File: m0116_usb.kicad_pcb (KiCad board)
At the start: 2 copper layers, 372.1 x 113.8 mm, 184 parts, among them J1 AVR-ISP-6, J2 Conn_01x04, J3 Conn_01x04, U1 ATmega32A-PU

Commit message: change ucontroller to ATmega32u4
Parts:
- D10, D11, D12, D13, D14, D15, D16, D17, D18, D19, D20, D21, D22, D23, D24, D25, D26, D27, D28, D29, D3, D30, D31, D32, D33, D34, D35, D36, D37, D38, D39, D4, D40, D41, D42, D43, D44, D45, D46, D47, D48, D49, D5, D50, D51, D52, D53, D54, D55, D56, D57, D58, D59, D6, D60, D61, D62, D63, D64, D65, D66, D67, D68, D69, D7, D70, D71, D72, D73, D74, D75, D76, D77, D78, D79, D8, D80, D81, D82, D83, D9: footprint Diode_THT:D_DO-35_SOD27_P7.62mm_Horizontal -> Diode_SMD:D_SOD-123
- MX1, MX10, MX11, MX12, MX13, MX14, MX15, MX16, MX17, MX18, MX19, MX2, MX20, MX21, MX22, MX23, MX24, MX25, MX26, MX27, MX28, MX29, MX3, MX30, MX31, MX32, MX33, MX34, MX35, MX36, MX37, MX38, MX39, MX4, MX40, MX41, MX42, MX43, MX44, MX45, MX46, MX47, MX48, MX49, MX5, MX50, MX51, MX52, MX53, MX54, MX55, MX56, MX57, MX58, MX59, MX6, MX60, MX61, MX62, MX63, MX64, MX65, MX66, MX67, MX68, MX69, MX7, MX70, MX71, MX72, MX73, MX74, MX75, MX76, MX77, MX78, MX79, MX8, MX80, MX81, MX9: footprint Alps_Only:ALPS-1U -> project_custom_parts:ALPS-1U
- USB1: footprint random-keyboard-parts:Molex-0548190519 -> project_custom_parts:Molex-0548190519
- renumbered Boot to Boot1, Reset to Reset1
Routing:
- net row4: track 532.5 -> 502.9 mm
- net Net-(D74-Pad2): track 6.94 -> 0.48 mm

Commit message: populate smd components, routing, finalize rev2
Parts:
- removed Boot1: Boot, Button_Switch_THT:SW_PUSH_6mm
- removed the D11 at (196.3, 112.0)
- removed the D2 at (75.4, 89.4)
- removed the D3 at (43.9, 112.0)
- removed D83: D_Small, Diode_SMD:D_SOD-123
- removed MX1, MX10, MX11, MX12, MX13, MX14, MX15, MX16, MX17, MX18, MX19, MX2, MX20, MX21, MX22, MX23, MX24, MX25, MX26, MX27, MX28, MX29, MX3, MX30, MX31, MX32, MX33, MX34, MX35, MX36, MX37, MX38, MX39, MX4, MX40, MX41, MX42, MX43, MX44, MX45, MX46, MX47, MX48, MX49, MX5, MX50, MX51, MX52, MX53, MX54, MX55, MX56, MX57, MX58, MX59, MX6, MX60, MX61, MX62, MX63, MX64, MX65, MX66, MX67, MX68, MX69, MX7, MX70, MX71, MX72, MX73, MX74, MX75, MX76, MX77, MX78, MX79, MX8, MX80, MX81, MX9: MX-NoLED, project_custom_parts:ALPS-1U
- removed Reset1: Reset, Button_Switch_THT:SW_PUSH_6mm
- removed USB1: USB_B_Mini, project_custom_parts:Molex-0548190519
- removed XTAL1: Crystal, Crystal:Crystal_HC49-4H_Vertical
- added C6: 22p, Capacitor_SMD:C_0402_1005Metric, F.Cu at (175.8, 86.2)
- added C7: 22p, Capacitor_SMD:C_0402_1005Metric, F.Cu at (173.5, 83.8)
- added C8: 1u, Capacitor_SMD:C_0402_1005Metric, F.Cu at (185.8, 77.8)
- added D81: D_Small, Diode_SMD:D_SOD-123, F.Cu at (381.0, 160.2)
- added D9: D_Small, Diode_SMD:D_SOD-123, F.Cu at (196.2, 102.2)
- added G***: LOGO, project_custom_parts:alps_logo, F.Cu at (288.0, 81.5)
- added J4: AVR-ISP-6, Connector_IDC:IDC-Header_2x03_P2.54mm_Vertical, F.Cu at (259.5, 77.5)
- added JP1: Jumper_NC_Dual, Jumper:SolderJumper-3_P1.3mm_Bridged12_Pad1.0x1.5mm, F.Cu at (245.8, 80.0)
- added K1: ESC, project_custom_parts:ALPS-1U, F.Cu at (34.4, 102.5)
- added K10: 9, project_custom_parts:ALPS-1U, F.Cu at (205.9, 102.5)
- added K11: 0, project_custom_parts:ALPS-1U, F.Cu at (224.9, 102.5)
- added K12: -, project_custom_parts:ALPS-1U, F.Cu at (244.1, 102.5)
- added K13: =, project_custom_parts:ALPS-1U, F.Cu at (263.3, 102.5)
- added K14: backspace, project_custom_parts:ALPS-1U, F.Cu at (287.4, 102.5)
- added K15: num_clear, project_custom_parts:ALPS-1U, F.Cu at (329.9, 102.5)
- added K16: =, project_custom_parts:ALPS-1U, F.Cu at (349.0, 102.5)
- added K17: /, project_custom_parts:ALPS-1U, F.Cu at (368.1, 102.5)
- added K18: *, project_custom_parts:ALPS-1U, F.Cu at (387.2, 102.5)
- added K19: tab, project_custom_parts:ALPS-1U, F.Cu at (39.0, 121.5)
- added K2: 1, project_custom_parts:ALPS-1U, F.Cu at (53.3, 102.5)
- added K20: Q, project_custom_parts:ALPS-1U, F.Cu at (62.7, 121.5)
- added K21: W, project_custom_parts:ALPS-1U, F.Cu at (81.7, 121.5)
- added K22: E, project_custom_parts:ALPS-1U, F.Cu at (100.7, 121.5)
- added K23: R, project_custom_parts:ALPS-1U, F.Cu at (119.8, 121.5)
- added K24: T, project_custom_parts:ALPS-1U, F.Cu at (138.9, 121.5)
- added K25: Y, project_custom_parts:ALPS-1U, F.Cu at (158.0, 121.5)
- added K26: U, project_custom_parts:ALPS-1U, F.Cu at (177.2, 121.5)
- added K27: I, project_custom_parts:ALPS-1U, F.Cu at (196.2, 121.5)
- added K28: O, project_custom_parts:ALPS-1U, F.Cu at (215.4, 121.5)
- added K29: P, project_custom_parts:ALPS-1U, F.Cu at (234.7, 121.5)
- added K3: 2, project_custom_parts:ALPS-1U, F.Cu at (72.3, 102.5)
- added K30: [, project_custom_parts:ALPS-1U, F.Cu at (253.7, 121.5)
- added K31: ], project_custom_parts:ALPS-1U, F.Cu at (272.8, 121.5)
- added K32: enter, project_custom_parts:ALPS-1U, F.Cu at (292.0, 131.9)
- added K33: num_7, project_custom_parts:ALPS-1U, F.Cu at (329.9, 121.5)
- added K34: num_8, project_custom_parts:ALPS-1U, F.Cu at (349.0, 121.5)
- added K35: num_9, project_custom_parts:ALPS-1U, F.Cu at (368.1, 121.5)
- added K36: +, project_custom_parts:ALPS-1U, F.Cu at (387.2, 121.5)
- added K37: control, project_custom_parts:ALPS-1U, F.Cu at (41.1, 140.6)
- added K38: A, project_custom_parts:ALPS-1U, F.Cu at (67.3, 140.6)
- added K39: S, project_custom_parts:ALPS-1U, F.Cu at (86.4, 140.6)
- added K4: 3, project_custom_parts:ALPS-1U, F.Cu at (91.2, 102.5)
- added K40: D, project_custom_parts:ALPS-1U, F.Cu at (105.4, 140.6)
- added K41: F, project_custom_parts:ALPS-1U, F.Cu at (124.5, 140.6)
- added K42: G, project_custom_parts:ALPS-1U, F.Cu at (143.6, 140.6)
- added K43: H, project_custom_parts:ALPS-1U, F.Cu at (162.7, 140.6)
- added K44: J, project_custom_parts:ALPS-1U, F.Cu at (181.9, 140.6)
- added K45: K, project_custom_parts:ALPS-1U, F.Cu at (201.0, 140.6)
- added K46: L, project_custom_parts:ALPS-1U, F.Cu at (220.1, 140.6)
- added K47: ;, project_custom_parts:ALPS-1U, F.Cu at (239.3, 140.6)
- added K48: ', project_custom_parts:ALPS-1U, F.Cu at (258.4, 140.6)
- added K49: num_4, project_custom_parts:ALPS-1U, F.Cu at (329.9, 140.6)
- added K5: 4, project_custom_parts:ALPS-1U, F.Cu at (110.2, 102.5)
- added K50: num_5, project_custom_parts:ALPS-1U, F.Cu at (349.0, 140.6)
- added K51: num_6, project_custom_parts:ALPS-1U, F.Cu at (368.1, 140.6)
- added K52: -, project_custom_parts:ALPS-1U, F.Cu at (387.2, 140.6)
- added K53: shift, project_custom_parts:ALPS-1U, F.Cu at (46.2, 159.9)
- added K54: Z, project_custom_parts:ALPS-1U, F.Cu at (76.8, 159.9)
- added K55: X, project_custom_parts:ALPS-1U, F.Cu at (95.9, 159.9)
- added K56: C, project_custom_parts:ALPS-1U, F.Cu at (115.1, 159.9)
- added K57: V, project_custom_parts:ALPS-1U, F.Cu at (134.1, 159.9)
- added K58: B, project_custom_parts:ALPS-1U, F.Cu at (153.3, 159.9)
- added K59: N, project_custom_parts:ALPS-1U, F.Cu at (172.5, 159.9)
- added K6: 5, project_custom_parts:ALPS-1U, F.Cu at (129.3, 102.5)
- added K60: M, project_custom_parts:ALPS-1U, F.Cu at (191.5, 159.9)
- added K61: ,, project_custom_parts:ALPS-1U, F.Cu at (210.7, 159.9)
- added K62: ., project_custom_parts:ALPS-1U, F.Cu at (229.7, 159.9)
- added K63: /, project_custom_parts:ALPS-1U, F.Cu at (248.9, 159.9)
- added K64: r_shift, project_custom_parts:ALPS-1U, F.Cu at (280.0, 159.9)
- added K65: num_1, project_custom_parts:ALPS-1U, F.Cu at (329.9, 159.9)
- added K66: num_2, project_custom_parts:ALPS-1U, F.Cu at (349.0, 159.9)
- added K67: num_3, project_custom_parts:ALPS-1U, F.Cu at (368.1, 159.9)
- added K68: capslock, project_custom_parts:ALPS-1U, F.Cu at (34.2, 178.9)
- added K69: option, project_custom_parts:ALPS-1U, F.Cu at (53.1, 178.9)
- added K7: 6, project_custom_parts:ALPS-1U, F.Cu at (148.3, 102.5)
- added K70: mac, project_custom_parts:ALPS-1U, F.Cu at (79.1, 178.9)
- added K71: ~~, project_custom_parts:ALPS-1U, F.Cu at (105.4, 178.9)
- added K72: long_sw, project_custom_parts:ALPS-1U, F.Cu at (139.1, 79.5)
- added K73: space, project_custom_parts:ALPS-1U, F.Cu at (185.9, 178.9)
- added K74: \, project_custom_parts:ALPS-1U, F.Cu at (215.4, 178.9)
- added K75: left, project_custom_parts:ALPS-1U, F.Cu at (234.4, 178.9)
- added K76: right, project_custom_parts:ALPS-1U, F.Cu at (253.6, 178.9)
- added K77: down, project_custom_parts:ALPS-1U, F.Cu at (272.8, 178.9)
- added K78: up, project_custom_parts:ALPS-1U, F.Cu at (291.8, 178.9)
- added K79: num_0, project_custom_parts:ALPS-1U, F.Cu at (339.6, 178.9)
- added K8: 7, project_custom_parts:ALPS-1U, F.Cu at (167.5, 102.5)
- added K80: ., project_custom_parts:ALPS-1U, F.Cu at (368.1, 178.9)
- added K81: enter, project_custom_parts:ALPS-1U, F.Cu at (387.2, 170.2)
- added K9: 8, project_custom_parts:ALPS-1U, F.Cu at (186.7, 102.5)
- added R5: 22, Resistor_SMD:R_0603_1608Metric, F.Cu at (179.0, 75.2)
- added R6: 22, Resistor_SMD:R_0603_1608Metric, F.Cu at (179.0, 76.7)
- added SW1: Reset, Button_Switch_SMD:SW_SPST_TL3342, F.Cu at (162.4, 87.0)
- added U2: USBLC6-2SC6, Package_TO_SOT_SMD:SOT-23-6, F.Cu at (72.8, 83.6)
- added X1: Crystal, Crystal:Crystal_SMD_3225-4Pin_3.2x2.5mm, F.Cu at (175.8, 83.8)
- C1: value 4.7u -> 0.1u; footprint Capacitor_THT:CP_Radial_D5.0mm_P2.50mm -> Capacitor_SMD:C_0603_1608Metric
- C2, C3: footprint Capacitor_THT:C_Disc_D3.0mm_W2.0mm_P2.50mm -> Capacitor_SMD:C_0603_1608Metric
- C4: value 22p -> 0.1u; footprint Capacitor_THT:C_Disc_D6.0mm_W2.5mm_P5.00mm -> Capacitor_SMD:C_0603_1608Metric
- C5: value 22p -> 10u; footprint Capacitor_THT:C_Disc_D6.0mm_W2.5mm_P5.00mm -> Capacitor_SMD:C_0603_1608Metric
- D1: value 3.6V -> D_Small; footprint Diode_THT:D_DO-35_SOD27_P7.62mm_Horizontal -> Diode_SMD:D_SOD-123
- F1: footprint Fuse:Fuse_Littelfuse_395Series -> Fuse:Fuse_1206_3216Metric_Castellated
- J1: value AVR-ISP-6 -> USB_C_port; footprint Connector_PinHeader_2.54mm:PinHeader_2x03_P2.54mm_Horizontal -> Connector_USB:USB_C_Receptacle_XKB_U262-16XN-4BVC11
- J2: footprint Connector_PinHeader_2.00mm:PinHeader_1x04_P2.00mm_Vertical -> Connector_PinHeader_1.00mm:PinHeader_1x04_P1.00mm_Vertical
- J3: footprint Connector_JST:JST_PH_S4B-PH-K_1x04_P2.00mm_Horizontal -> project_custom_parts:PinSocket_1x04_P1.00mm_Vertical_SMD
- R1: footprint Resistor_THT:R_Axial_DIN0207_L6.3mm_D2.5mm_P10.16mm_Horizontal -> Resistor_SMD:R_0603_1608Metric
- R2: value 1.5k -> 10k; footprint Resistor_THT:R_Axial_DIN0207_L6.3mm_D2.5mm_P10.16mm_Horizontal -> Resistor_SMD:R_0603_1608Metric
- R3, R4: value 68R -> 5.1k; footprint Resistor_THT:R_Axial_DIN0207_L6.3mm_D2.5mm_P10.16mm_Horizontal -> Resistor_SMD:R_0402_1005Metric
- U1: value ATmega32A-PU -> ATmega32U4-AU; footprint Package_DIP:DIP-40_W15.24mm_Socket -> Package_QFP:TQFP-44_10x10mm_P0.8mm
- moved J1 295.8 mm to (46.2, 80.2), turned to 270 degrees
- moved C2 199.6 mm to (77.5, 80.2), turned to 0 degrees
- moved R4 139.0 mm to (51.6, 81.8), turned to 180 degrees
- moved R3 134.2 mm to (51.6, 78.8), turned to 0 degrees
- moved U1 118.1 mm to (185.5, 84.8)
- moved C3 87.7 mm to (193.0, 81.2), turned to 270 degrees
- moved R1 73.4 mm to (156.5, 85.8), turned to 270 degrees
- moved C4 71.3 mm to (181.2, 92.2)
- moved C5 57.9 mm to (192.8, 90.7), turned to 270 degrees
- moved D1 35.5 mm to (43.9, 102.2), turned to 270 degrees
- moved C1 14.8 mm to (72.7, 87.2), turned to 180 degrees
- moved R2 13.8 mm to (190.8, 91.3), turned to 90 degrees
- moved D13 9.82 mm to (272.8, 102.2), turned to 270 degrees
- moved D15 9.77 mm to (320.5, 102.2), turned to 270 degrees
- moved D14 9.77 mm to (298.2, 102.2), turned to 270 degrees
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- renumbered D12 to D10, D13 to D11, D14 to D12, D15 to D13, D16 to D14, D17 to D15, D18 to D16, D19 to D17, D20 to D18, D21 to D19, D4 to D2, D22 to D20, D23 to D21, D24 to D22, D25 to D23, D26 to D24, D27 to D25, D28 to D26, D29 to D27, D30 to D28, D31 to D29, D5 to D3, D32 to D30, D33 to D31, D34 to D32, D35 to D33, D36 to D34, D37 to D35, D38 to D36, D39 to D37, D40 to D38, D41 to D39, D6 to D4, D42 to D40, D43 to D41, D44 to D42, D45 to D43, D46 to D44, D47 to D45, D48 to D46, D49 to D47, D50 to D48, D51 to D49, D7 to D5, D52 to D50, D53 to D51, D54 to D52, D55 to D53, D56 to D54, D57 to D55, D58 to D56, D59 to D57, D60 to D58, D61 to D59, D8 to D6, D62 to D60, D63 to D61, D64 to D62, D65 to D63, D66 to D64, D67 to D65, D68 to D66, D69 to D67, D70 to D68, D71 to D69, D9 to D7, D72 to D70, D73 to D71, D74 to D72, D75 to D73, D76 to D74, D77 to D75, D78 to D76, D79 to D77, D80 to D78, D81 to D79, D10 to D8, D82 to D80
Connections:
- C4 pad 1: Net-(C4-Pad1) -> +5V
- C5 pad 1: Net-(C5-Pad1) -> +5V
- D1 pad 1: Net-(D1-Pad1) -> row1
- D1 pad 2: GND -> Net-(D1-Pad2)
- D10 pad 1: row0 -> row1
- D11 pad 1: row0 -> row1
- D12 pad 1: row0 -> row1
- D13 pad 1: row0 -> row1
- D14 pad 1: row0 -> row1
- D15 pad 1: row0 -> row1
- D16 pad 1: row0 -> row1
- D17 pad 1: row0 -> row1
- D18 pad 1: row0 -> row1
- D19 pad 1: row1 -> row2
- D2 pad 1: row0 -> row1
- D20 pad 1: row1 -> row2
- D21 pad 1: row1 -> row2
- D22 pad 1: row1 -> row2
- D23 pad 1: row1 -> row2
- D24 pad 1: row1 -> row2
- D25 pad 1: row1 -> row2
- D26 pad 1: row1 -> row2
- D27 pad 1: row1 -> row2
- D28 pad 1: row1 -> row2
- D29 pad 1: row1 -> row2
- D3 pad 1: row0 -> row1
- D30 pad 1: row1 -> row2
- D31 pad 1: row1 -> row2
- D32 pad 1: row1 -> row2
- D33 pad 1: row1 -> row2
- D34 pad 1: row1 -> row2
- D35 pad 1: row1 -> row2
- D36 pad 1: row1 -> row2
- D37 pad 1: row2 -> row3
- D38 pad 1: row2 -> row3
- D39 pad 1: row2 -> row3
- D4 pad 1: row0 -> row1
- D40 pad 1: row2 -> row3
- D41 pad 1: row2 -> row3
- D42 pad 1: row2 -> row3
- D43 pad 1: row2 -> row3
- D44 pad 1: row2 -> row3
- D45 pad 1: row2 -> row3
- D46 pad 1: row2 -> row3
- D47 pad 1: row2 -> row3
- D48 pad 1: row2 -> row3
- D49 pad 1: row2 -> row3
- D5 pad 1: row0 -> row1
- D50 pad 1: row2 -> row3
- D51 pad 1: row2 -> row3
- D52 pad 1: row2 -> row3
- D53 pad 1: row3 -> row4
- D54 pad 1: row3 -> row4
- D55 pad 1: row3 -> row4
- D56 pad 1: row3 -> row4
- D57 pad 1: row3 -> row4
- D58 pad 1: row3 -> row4
- D59 pad 1: row3 -> row4
- D6 pad 1: row0 -> row1
- D60 pad 1: row3 -> row4
- D61 pad 1: row3 -> row4
- D62 pad 1: row3 -> row4
- D63 pad 1: row3 -> row4
- D64 pad 1: row3 -> row4
- D65 pad 1: row3 -> row4
- D66 pad 1: row3 -> row4
- D67 pad 1: row3 -> row4
- D68 pad 1: row4 -> row5
- D69 pad 1: row4 -> row5
- D7 pad 1: row0 -> row1
- D70 pad 1: row4 -> row5
- D71 pad 1: row4 -> row5
- D73 pad 1: row4 -> row5
- D74 pad 1: row4 -> row5
- D75 pad 1: row4 -> row5
- D76 pad 1: row4 -> row5
- D77 pad 1: row4 -> row5
- D78 pad 1: row4 -> row5
- D79 pad 1: row4 -> row5
- D8 pad 1: row0 -> row1
- D80 pad 1: row4 -> row5
- J2 pad 2: Net-(J2-Pad2) -> Net-(J1-PadA7)
- J2 pad 3: Net-(J2-Pad3) -> Net-(J1-PadA6)
- J3 pad 2: Net-(D1-Pad1) -> CONN_D-
- J3 pad 3: Net-(D2-Pad1) -> CONN_D+
- R1 pad 1: +5V -> reset
- R1 pad 2: reset -> +5V
- R2 pad 1: Net-(D2-Pad1) -> GND
- R2 pad 2: +5V -> Net-(R2-Pad2)
- R3 pad 1: Net-(D1-Pad1) -> Net-(J1-PadA5)
- R3 pad 2: D+ -> GND
- R4 pad 1: Net-(D2-Pad1) -> GND
- R4 pad 2: D- -> Net-(J1-PadB5)
- U1 pad 1: Net-(U1-Pad1) -> row4
- U1 pad 10: +5V -> MOSI
- U1 pad 11: GND -> MISO
- U1 pad 12: Net-(C5-Pad1) -> col1
- U1 pad 13: Net-(C4-Pad1) -> reset
- U1 pad 14: col4 -> +5V
- U1 pad 15: col3 -> GND
- U1 pad 16: D+ -> XTAL2
- U1 pad 17: D- -> XTAL1
- U1 pad 18: boot -> col2
- U1 pad 19: col2 -> col3
- U1 pad 2: row0 -> +5V
- U1 pad 20: col1 -> col4
- U1 pad 21: col5 -> col7
- U1 pad 22: col6 -> col5
- U1 pad 23: col7 -> GND
- U1 pad 24: col8 -> +5V
- U1 pad 25: col9 -> col18
- U1 pad 26: col10 -> col8
- U1 pad 27: col11 -> col9
- U1 pad 28: col12 -> col10
- U1 pad 29: col13 -> col11
- U1 pad 3: row1 -> D-
- U1 pad 30: +5V -> col12
- U1 pad 31: GND -> col14
- U1 pad 32: Net-(U1-Pad32) -> col15
- U1 pad 33: col14 -> Net-(R2-Pad2)
- U1 pad 34: col15 -> +5V
- U1 pad 35: col16 -> GND
- U1 pad 36: col17 -> row1
- U1 pad 37: col18 -> row2
- U1 pad 39: row4 -> row5
- U1 pad 4: Net-(U1-Pad4) -> D+
- U1 pad 40: row2 -> col16
- U1 pad 5: Net-(U1-Pad5) -> GND
- U1 pad 6: MOSI -> Net-(C8-Pad1)
- U1 pad 7: MISO -> +5V
- U1 pad 8: SCK -> col6
- U1 pad 9: reset -> boot_jp
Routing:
- net row5: track 0.00 -> 525.7 mm, vias 0 -> 2
- net row0: track 382.4 -> 0.00 mm
- net +5V: track 353.9 -> 16.7 mm, vias 0 -> 11
- net Net-(D2-Pad1): track 144.4 -> 0.00 mm
- net Net-(D1-Pad1): track 130.4 -> 0.00 mm
- net col18: track 176.8 -> 305.7 mm, vias 0 -> 2
- net /D1+: track 0.00 -> 109.1 mm
- net /D1-: track 0.00 -> 109.1 mm
- net col15: track 127.7 -> 232.2 mm, vias 0 -> 1
- net col17: track 159.5 -> 262.8 mm, vias 0 -> 1
- net col16: track 122.3 -> 224.8 mm, vias 0 -> 1
- net col4: track 275.2 -> 174.5 mm, vias 0 -> 1
- net col3: track 294.4 -> 196.5 mm, vias 0 -> 1
- net col14: track 95.4 -> 191.0 mm, vias 0 -> 1
- net col2: track 309.7 -> 219.6 mm, vias 0 -> 1
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- added copper zone on In2.Cu, net +5V
- added copper zone on In1.Cu, net GND
- added copper zone on In2.Cu, net VCC
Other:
- outline, holes or cut-outs redrawn
- copper layers 2 -> 4
- board text added: "Debugging space"
- board text added: "This is alps board!"
- board text added: "github.com/hyp3d"
- board text removed: "github.com/kb-elmo/m0116_usb elmo.space"
- board text removed: "nice"

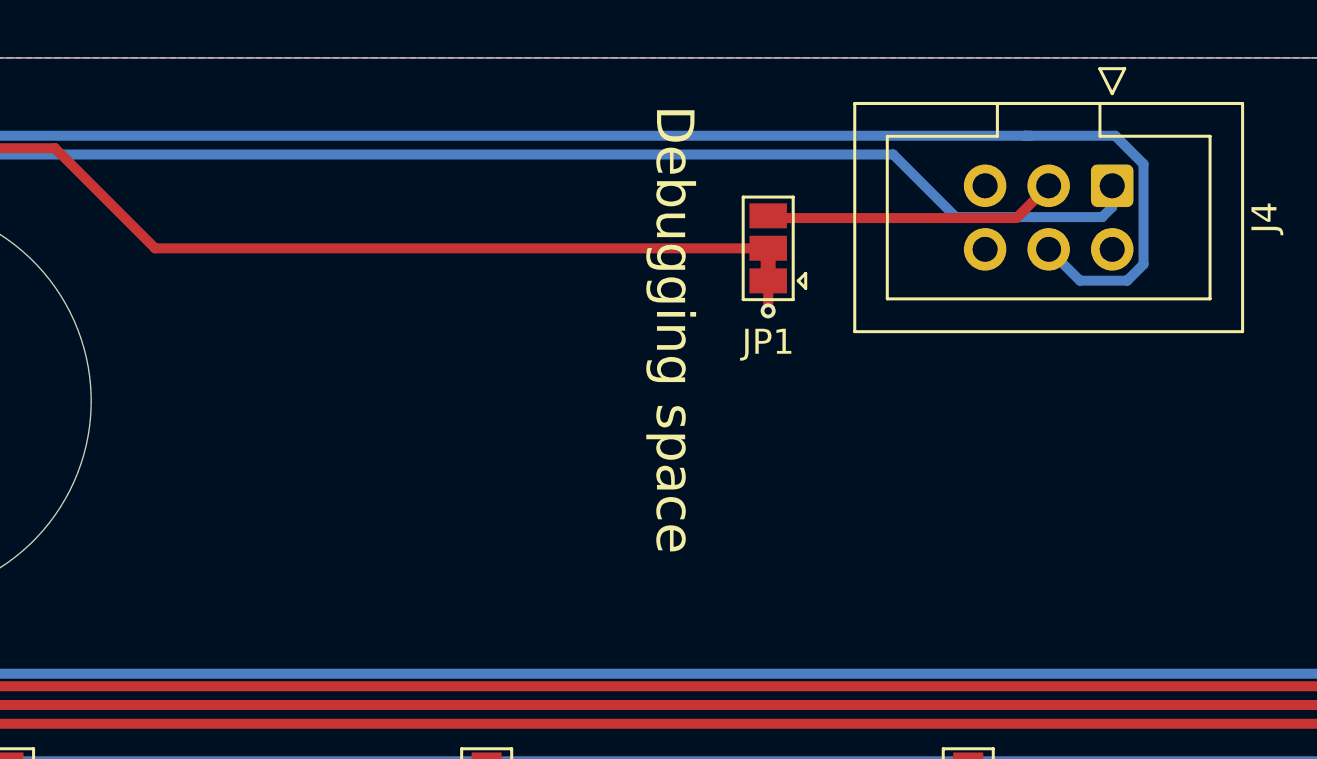
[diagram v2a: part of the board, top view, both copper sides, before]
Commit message: replace smd jumper with spdt switch
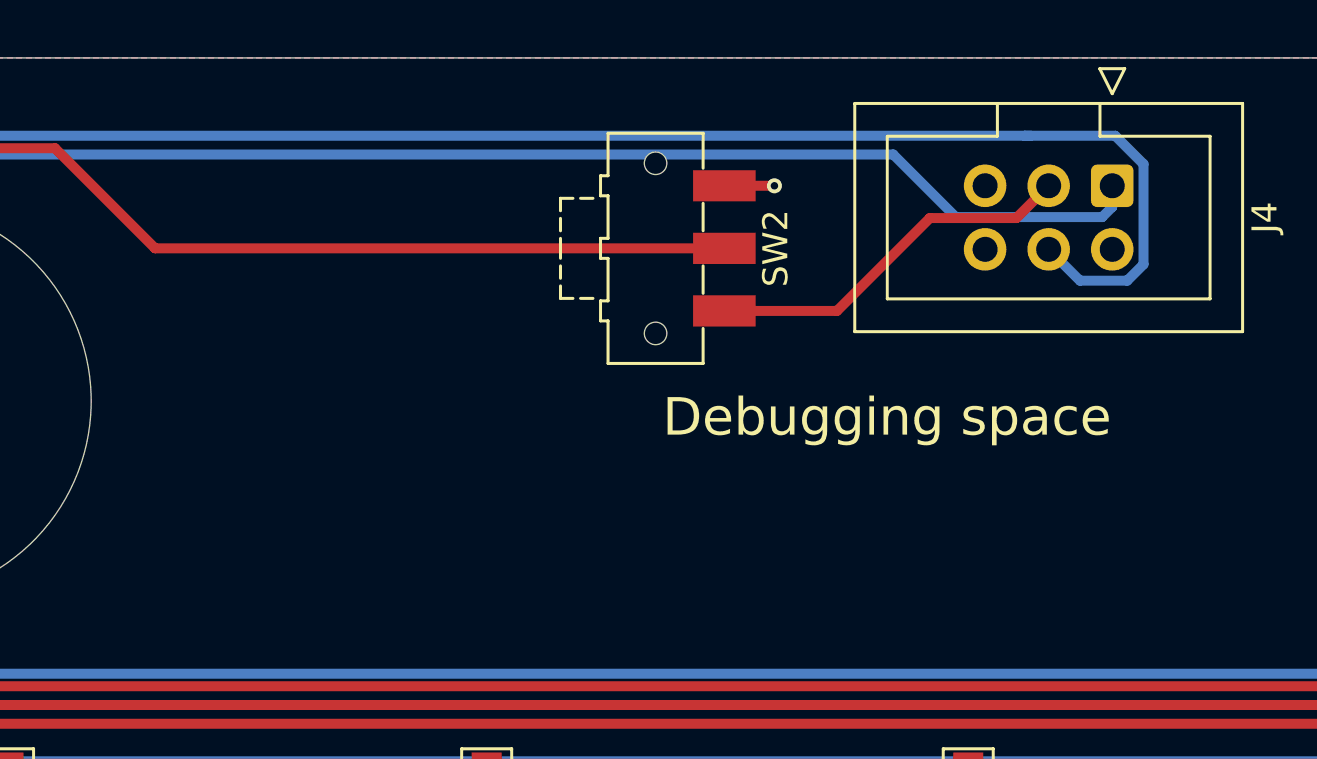
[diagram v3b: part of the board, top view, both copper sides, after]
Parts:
- removed JP1: Jumper_NC_Dual, Jumper:SolderJumper-3_P1.3mm_Bridged12_Pad1.0x1.5mm
- added SW2: SW_SPDT, Button_Switch_SMD:SW_SPDT_CK-JS102011SAQN, F.Cu at (241.2, 80.0)
- moved G*** 3.00 mm to (152.6, 170.6)
- moved G*** 3.00 mm to (129.6, 170.8)
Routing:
- net col13: track 56.6 -> 62.6 mm
- net SCK: track 11.8 -> 15.0 mm
- net boot_jp: track 67.7 -> 65.9 mm

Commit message: revise daughterboard, finalize
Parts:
- G***: moved to B.Cu
- SW2: footprint Button_Switch_SMD:SW_SPDT_CK-JS102011SAQN -> project_custom_parts:SW_SPDT_SK-3245S-L1-A
- moved R1 110.6 mm to (267.0, 80.1)
- moved SW1 99.2 mm to (261.5, 81.2)
- moved G*** 75.6 mm to (306.5, 154.8), turned to 180 degrees
- moved J4 29.8 mm to (289.2, 79.2)
- moved C1 21.5 mm to (51.2, 86.0), turned to 90 degrees
- moved F1 20.7 mm to (52.8, 76.0)
- moved U2 20.5 mm to (52.5, 80.2)
- moved J2 7.75 mm to (54.0, 86.5), turned to 180 degrees
- moved C2 6.10 mm to (71.7, 82.1)
- moved SW2 1.75 mm to (241.2, 81.8)
- moved R4 1.65 mm to (51.2, 83.4), turned to 90 degrees
- moved R3 1.01 mm to (52.1, 77.9)
- moved C7 0.95 mm to (173.8, 82.8)
- moved J1 0.50 mm to (45.8, 80.2)
- moved C6 0.35 mm to (176.0, 86.0)
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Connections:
- J1 pad A6: Net-(J1-PadA6) -> USB_D+
- J1 pad B6: Net-(J1-PadA6) -> USB_D+
- J2 pad 1: VCC -> +5V
- J2 pad 2: Net-(J1-PadA7) -> CONN_D-
- J2 pad 3: Net-(J1-PadA6) -> CONN_D+
- J3 pad 1: VCC -> +5V
- J3 pad 2: CONN_D- -> D-
- J3 pad 3: CONN_D+ -> D+
- R5 pad 1: /D1- -> D-
- R5 pad 2: D- -> Net-(R5-Pad2)
- R6 pad 2: /D1+ -> Net-(R6-Pad2)
- U1 pad 3: D- -> Net-(R5-Pad2)
- U1 pad 4: D+ -> Net-(R6-Pad2)
- U2 pad 1: CONN_D- -> Net-(J1-PadA7)
- U2 pad 3: CONN_D+ -> USB_D+
- U2 pad 4: /D1+ -> CONN_D+
- U2 pad 6: /D1- -> CONN_D-
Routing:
- net /D1+: track 109.1 -> 0.00 mm
- net /D1-: track 109.1 -> 0.00 mm
- net D+: track 9.99 -> 113.9 mm
- net D-: track 10.9 -> 113.9 mm
- net reset: track 103.3 -> 134.8 mm
- net SCK: track 15.0 -> 46.2 mm
- net MOSI: track 91.7 -> 120.7 mm
- net MISO: track 84.2 -> 113.2 mm
- net Net-(R5-Pad2): track 0.00 -> 10.9 mm
- net Net-(R6-Pad2): track 0.00 -> 9.99 mm
- net Net-(J1-PadA6): track 6.12 -> 0.00 mm
- net CONN_D-: track 3.08 -> 8.06 mm
- net GND: track 15.1 -> 19.1 mm, vias 22 -> 18
- net USB_D+: track 0.00 -> 4.00 mm
- net +5V: track 16.7 -> 20.2 mm, vias 11 -> 10
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- removed copper zone on In2.Cu, net VCC
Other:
- outline, holes or cut-outs redrawn
- board text added: "DEBUGGING MODE"
- board text added: "ISP"
- board text added: "JLCJCLJCLJCL"
- board text added: "JST SOCKET"
- board text added: "RESET"
- board text removed: "Debugging space"
